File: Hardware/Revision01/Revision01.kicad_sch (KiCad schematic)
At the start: 6 parts, among them J5 Conn_01x02

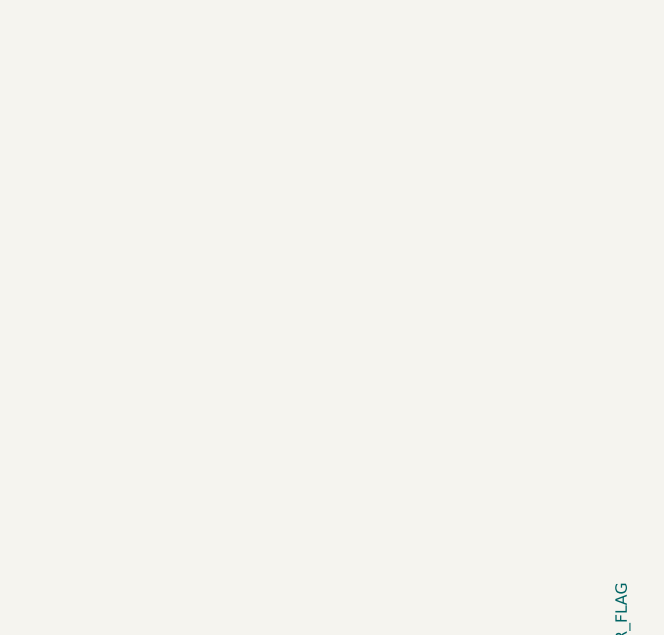
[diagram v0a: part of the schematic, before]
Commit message: footprint added for nucleo board
To do before PCB LAYOUT

clean up schematic
wire-accross sheets
Improve annotation ordering

Perform ERC check
Ensure all components have footprints
Create net classes
	POWER
	GND
	SPI
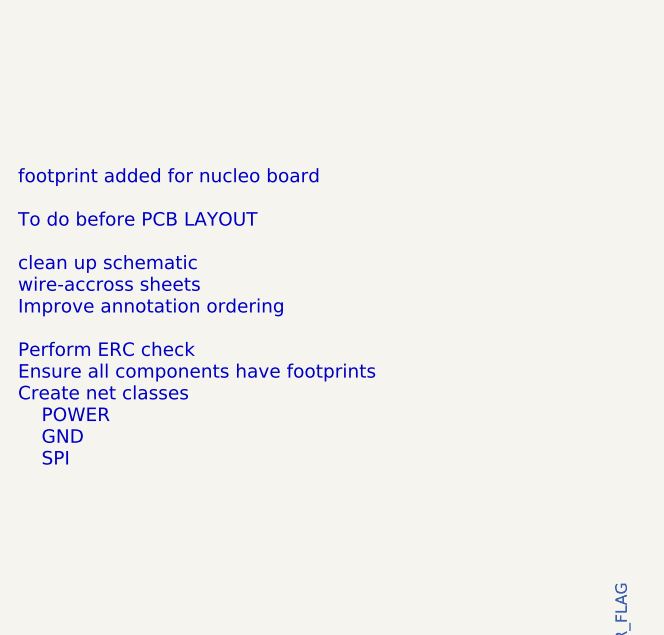
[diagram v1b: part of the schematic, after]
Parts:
- FID1, FID3: now in the parts list
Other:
- note added: "footprint added for nucleo board To do before PCB LAYOUT clean up schematic wire-accross sheets Improve annotation ordering Perform ERC check Ensure all components have footprints Create net classes POWER GND SPI"
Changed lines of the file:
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@@
 		(company "BCIT BAJA")
+	)
+	(text "\n\nfootprint added for nucleo board\n\nTo do before PCB LAYOUT\n\nclean up schematic\nwire-accross sheets\nImprove annotation ordering\n\nPerform ERC check\nEnsure all components have footprints\nCreate net classes\n	POWER\n	GND\n	SPI"
+		(exclude_from_sim no)
+		(at -45.466 99.568 0)
+		(effects
+			(font
+				(size 1.4986 1.4986)
+			)
+			(justify left)
+		)
 	)
 	(text "HOW MANY MOUNTING HOLES?"
@@
 		(at 161.29 189.23 0)
 		(unit 1)
-		(exclude_from_sim yes)
+		(exclude_from_sim no)
 		(in_bom no)
 		(on_board yes)
@@
 		(at 167.64 189.23 0)
 		(unit 1)
-		(exclude_from_sim yes)
-		(in_bom no)
+		(exclude_from_sim no)
+		(in_bom yes)
 		(on_board yes)
 		(dnp no)
@@
 		(at 153.67 189.23 0)
 		(unit 1)
-		(exclude_from_sim yes)
-		(in_bom no)
+		(exclude_from_sim no)
+		(in_bom yes)
 		(on_board yes)
 		(dnp no)

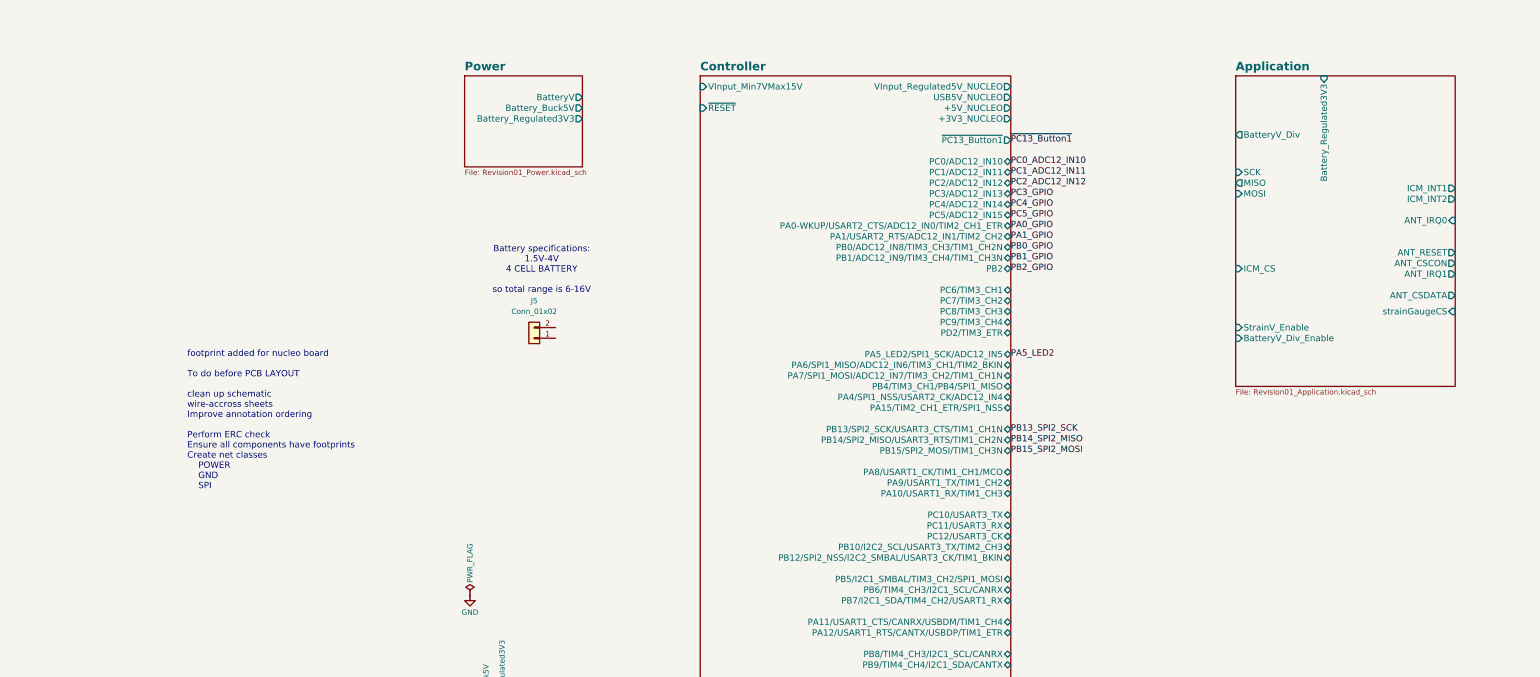
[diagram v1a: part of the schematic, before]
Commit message: started wiring modules together
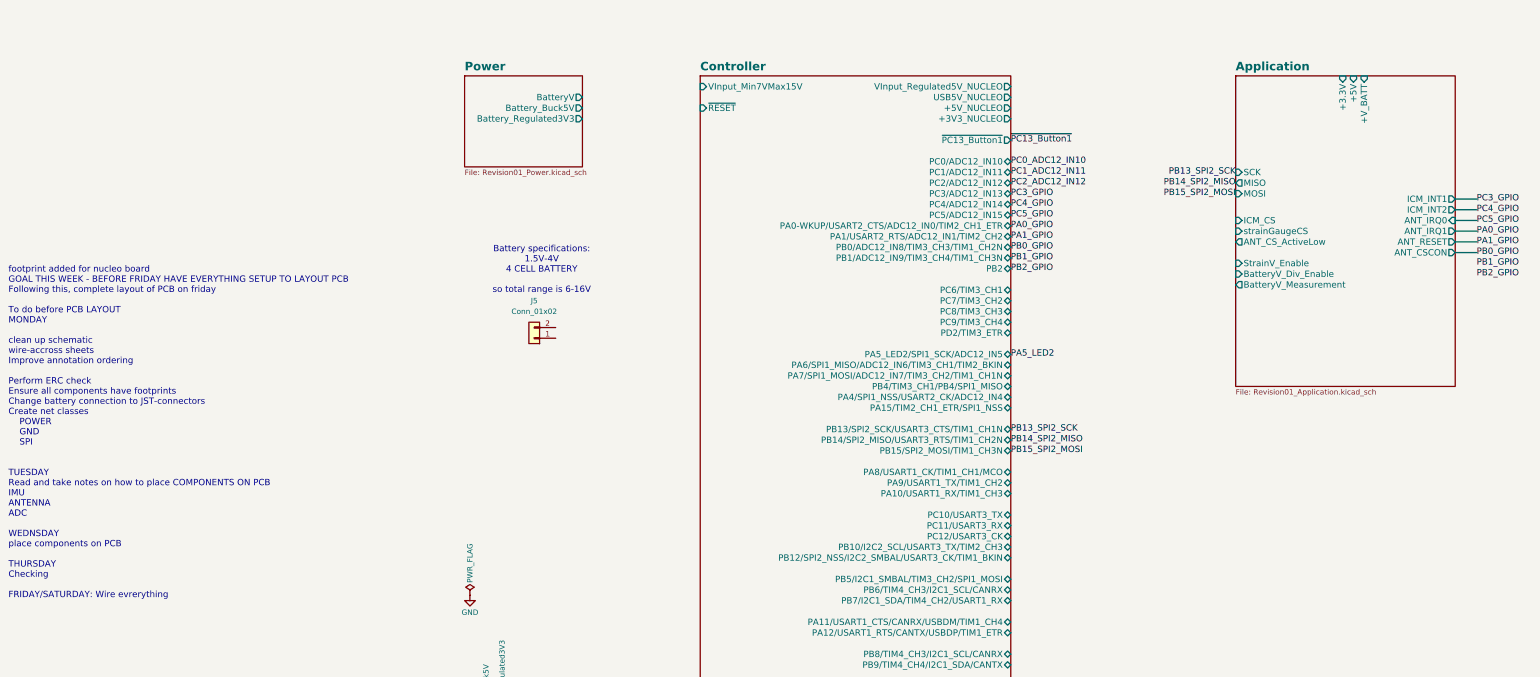
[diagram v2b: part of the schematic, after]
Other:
- sheet Application ports: added +3.3V, +5V, +V_BATT, ANT_CS_ActiveLow, BatteryV_Measurement; removed ANT_CSDATA, BatteryV_Div, Battery_Regulated3V3
- note added: "footprint added for nucleo board GOAL THIS WEEK - BEFORE FRIDAY HAVE EVERYTHING SETUP TO LAYOUT PCB Following this, complete layout of PCB on friday To do before PCB LAYOUT MONDAY clean up schematic wire-accross sheets Improve annotation ordering Perform ERC check Ensure all components have footprints Change battery connection to JST-connectors Create net classes POWER GND SPI TUESDAY Read and ta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"
- note removed: "footprint added for nucleo board To do before PCB LAYOUT clean up schematic wire-accross sheets Improve annotation ordering Perform ERC check Ensure all components have footprints Create net classes POWER GND SPI"
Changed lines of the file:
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@@
 		(company "BCIT BAJA")
 	)
-	(text "\n\nfootprint added for nucleo board\n\nTo do before PCB LAYOUT\n\nclean up schematic\nwire-accross sheets\nImprove annotation ordering\n\nPerform ERC check\nEnsure all components have footprints\nCreate net classes\n	POWER\n	GND\n	SPI"
-		(exclude_from_sim no)
-		(at -45.466 99.568 0)
+	(text "\n\nfootprint added for nucleo board\nGOAL THIS WEEK - BEFORE FRIDAY HAVE EVERYTHING SETUP TO LAYOUT PCB\nFollowing this, complete layout of PCB on friday\n\nTo do before PCB LAYOUT\nMONDAY\n\nclean up schematic\nwire-accross sheets\nImprove annotation ordering\n\nPerform ERC check\nEnsure all components have footprints\nChange battery connection to JST-connectors\nCreate net classes\n	POWER\n	GND\n	SPI\n\n\nTUESDAY\nRead and take notes on how to place COMPONENTS ON PCB\nIMU\nANTENNA\nADC\n\nWEDNSDAY \nplace components on PCB\n\nTHURSDAY\nChecking\n\nFRIDAY/SATURDAY: Wire evrerything\n\n\n"
+		(exclude_from_sim no)
+		(at -87.884 104.902 0)
 		(effects
 			(font
@@
 		(at 25.4 177.8)
 	)
+	(wire
+		(pts
+			(xy 260.35 59.69) (xy 255.27 59.69)
+		)
+		(stroke
+			(width 0)
+			(type default)
+		)
+	)
+	(wire
+		(pts
+			(xy 260.35 54.61) (xy 255.27 54.61)
+		)
+		(stroke
+			(width 0)
+			(type default)
+		)
+	)
+	(wire
+		(pts
+			(xy 260.35 57.15) (xy 255.27 57.15)
+		)
+		(stroke
+			(width 0)
+			(type default)
+		)
+	)
+	(wire
+		(pts
+			(xy 260.35 62.23) (xy 255.27 62.23)
+		)
+		(stroke
+			(width 0)
+			(type default)
+		)
+	)
+	(wire
+		(pts
+			(xy 260.35 49.53) (xy 255.27 49.53)
+		)
+		(stroke
+			(width 0)
+			(type default)
+		)
+	)
+	(wire
+		(pts
+			(xy 260.35 52.07) (xy 255.27 52.07)
+		)
+		(stroke
+			(width 0)
+			(type default)
+		)
+	)
 	(label "PC3_GPIO"
 		(at 149.86 48.26 0)
@@
 		)
 	)
+	(label "PB13_SPI2_SCK"
+		(at 203.2 43.18 180)
+		(effects
+			(font
+				(size 1.4986 1.4986)
+			)
+			(justify right)
+		)
+	)
 	(label "PB14_SPI2_MISO"
 		(at 149.86 106.68 0)
@@
 		)
 	)
+	(label "PA1_GPIO"
+		(at 260.35 59.69 0)
+		(effects
+			(font
+				(size 1.4986 1.4986)
+			)
+			(justify left)
+		)
+	)
+	(label "PC5_GPIO"
+		(at 260.35 54.61 0)
+		(effects
+			(font
+				(size 1.4986 1.4986)
+			)
+			(justify left)
+		)
+	)
+	(label "PA0_GPIO"
+		(at 260.35 57.15 0)
+		(effects
+			(font
+				(size 1.4986 1.4986)
+			)
+			(justify left)
+		)
+	)
+	(label "PB15_SPI2_MOSI"
+		(at 203.2 48.26 180)
+		(effects
+			(font
+				(size 1.4986 1.4986)
+			)
+			(justify right)
+		)
+	)
+	(label "PC4_GPIO"
+		(at 260.35 52.07 0)
+		(effects
+			(font
+				(size 1.4986 1.4986)
+			)
+			(justify left)
+		)
+	)
 	(label "PB0_GPIO"
 		(at 149.86 60.96 0)
@@
 		)
 	)
+	(label "PB14_SPI2_MISO"
+		(at 203.2 45.72 180)
+		(effects
+			(font
+				(size 1.4986 1.4986)
+			)
+			(justify right)
+		)
+	)
 	(label "PB1_GPIO"
 		(at 149.86 63.5 0)
@@
 		)
 	)
+	(label "PB2_GPIO"
+		(at 260.35 67.31 0)
+		(effects
+			(font
+				(size 1.4986 1.4986)
+			)
+			(justify left)
+		)
+	)
 	(label "PC0_ADC12_IN10"
 		(at 149.86 40.64 0)
@@
 		)
 	)
+	(label "PB0_GPIO"
+		(at 260.35 62.23 0)
+		(effects
+			(font
+				(size 1.4986 1.4986)
+			)
+			(justify left)
+		)
+	)
 	(label "PB2_GPIO"
 		(at 149.86 66.04 0)
@@
 	(label "PC1_ADC12_IN11"
 		(at 149.86 43.18 0)
+		(effects
+			(font
+				(size 1.4986 1.4986)
+			)
+			(justify left)
+		)
+	)
+	(label "PB1_GPIO"
+		(at 260.35 64.77 0)
+		(effects
+			(font
+				(size 1.4986 1.4986)
+			)
+			(justify left)
+		)
+	)
+	(label "PC3_GPIO"
+		(at 260.35 49.53 0)
 		(effects
 			(font
@@
 		)
 		(pin "ICM_INT1" output
-			(at 255.27 46.99 0)
+			(at 255.27 49.53 0)
 			(effects
 				(font
@@
 		)
 		(pin "ICM_INT2" output
-			(at 255.27 49.53 0)
+			(at 255.27 52.07 0)
 			(effects
 				(font
@@
 		)
 		(pin "ANT_RESET" output
+			(at 255.27 59.69 0)
+			(effects
+				(font
+					(size 1.4986 1.4986)
+				)
+				(justify right)
+			)
+		)
+		(pin "ANT_CSCON" output
 			(at 255.27 62.23 0)
 			(effects
@@
 			)
 		)
-		(pin "ANT_CSCON" output
-			(at 255.27 64.77 0)
-			(effects
-				(font
-					(size 1.4986 1.4986)
-				)
-				(justify right)
-			)
-		)
 		(pin "ANT_IRQ1" output
-			(at 255.27 67.31 0)
-			(effects
-				(font
-					(size 1.4986 1.4986)
-				)
-				(justify right)
-			)
-		)
-		(pin "ANT_CSDATA" output
-			(at 255.27 72.39 0)
+			(at 255.27 57.15 0)
 			(effects
 				(font
@@
 		)
 		(pin "strainGaugeCS" input
-			(at 255.27 76.2 0)
-			(effects
-				(font
-					(size 1.4986 1.4986)
-				)
-				(justify right)
-			)
-		)
-		(pin "Battery_Regulated3V3" input
-			(at 224.155 20.32 90)
-			(effects
-				(font
-					(size 1.4986 1.4986)
-				)
-				(justify right)
+			(at 203.2 57.15 180)
+			(effects
+				(font
+					(size 1.4986 1.4986)
+				)
+				(justify left)
 			)
 		)
 		(pin "ICM_CS" input
-			(at 203.2 66.04 180)
-			(effects
-				(font
-					(size 1.4986 1.4986)
-				)
-				(justify left)
-			)
-		)
-		(pin "BatteryV_Div" output
-			(at 203.2 34.29 180)
+			(at 203.2 54.61 180)
 			(effects
 				(font
@@
 		)
 		(pin "BatteryV_Div_Enable" input
-			(at 203.2 82.55 180)
+			(at 203.2 67.31 180)
 			(effects
 				(font
@@
 		)
 		(pin "StrainV_Enable" input
-			(at 203.2 80.01 180)
-			(effects
-				(font
+			(at 203.2 64.77 180)
+			(effects
+				(font
+					(size 1.4986 1.4986)
+				)
+				(justify left)
+			)
+		)
+		(pin "+3.3V" input
+			(at 228.6 20.32 90)
+			(effects
+				(font
+					(size 1.4986 1.4986)
+				)
+				(justify right)
+			)
+		)
+		(pin "+5V" input
+			(at 231.14 20.32 90)
+			(effects
+				(font
+					(size 1.4986 1.4986)
+				)
+				(justify right)
+			)
+		)
+		(pin "+V_BATT" input
+			(at 233.68 20.32 90)
+			(effects
+				(font
+					(size 1.4986 1.4986)
+				)
+				(justify right)
+			)
+		)
+		(pin "ANT_CS_ActiveLow" output
+			(at 203.2 59.69 180)
+			(effects
+				(font
+					(size 1.4986 1.4986)
+				)
+				(justify left)
+			)
+		)
+		(pin "BatteryV_Measurement" output
+			(at 203.2 69.85 180)
+			(effects
+				(font

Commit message: neated up the circuit - done wire-accross sheets - done Ensure all components have footprints - done Create net classes - DONE 	POWER 	GND 	SPI 	GPIO
Add in new components into BOM
	- Power switch, exclude from BOM - DONE - added component to switch. Not sure how to get it to work
	- Add in the resistors in parallel and series. for SPI busses - Done(PENDING whether to take series resistors out)
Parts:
- added H3, H4: MountingHole, MountingHole:MountingHole_3.2mm_M3, symbol Mechanical:MountingHole
- added R4, R5: 50, symbol Device:R
- added R6, R7: 10K, symbol Device:R
- added SW1: Power-switch connection, symbol Connector_Generic:Conn_01x02
- added TP16, TP17, TP18, TP19, TP8, TP9: TestPoint, TestPoint:TestPoint_THTPad_1.0x1.0mm_Drill0.5mm, symbol Connector:TestPoint
- H1, H2: footprint MountingHole:MountingHole_2.5mm -> MountingHole:MountingHole_3.2mm_M3
- J5: value Conn_01x02 -> Battery connector
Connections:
- net BatteryV: now also SW1.2 (Pin_2)
- net GND: now also J5.1 (Pin_1), TP19.1
- net at J5.2 (Pin_2): now also SW1.1 (Pin_1)
- new net +3.3V: R6.2, R7.2, TP8.1
- new net +5V: TP9.1
- new net Controller/PB14/SPI2_MISO/USART3_RTS/TIM1_CH2N: R4.1
- new net Controller/PB15/SPI2_MOSI/TIM1_CH3N: R5.1
- new net MISO: TP18.1
- new net MOSI: TP16.1
- new net SCK: TP17.1
- new net SPI_MISO: R4.2, R7.1
- new net SPI_MOSI: R5.2, R6.1
- no-connect marks 6 -> 7
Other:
- removed sheet Power
- sheet Application ports: added ANT_CSCON_AL, ANT_CS_DATA_AL; removed ANT_CSCON, ANT_CS_ActiveLow
- note added: "*Note this is externally connected wired to outside of case"
- note added: "These Mounting holes are M3"
- note added: "footprint added for nucleo board GOAL THIS WEEK - BEFORE FRIDAY HAVE EVERYTHING SETUP TO LAYOUT PCB Following this, complete layout of PCB on friday To do before PCB LAYOUT MONDAY Improve annotation ordering Perform ERC check TUESDAY Read and take notes on how to place COMPONENTS ON PCB IMU ANTENNA ADC WEDNSDAY place components on PCB THURSDAY Checking FRIDAY/SATURDAY: Wire evrerything"
- note removed: "HOW MANY MOUNTING HOLES?"
- note removed: "footprint added for nucleo board GOAL THIS WEEK - BEFORE FRIDAY HAVE EVERYTHING SETUP TO LAYOUT PCB Following this, complete layout of PCB on friday To do before PCB LAYOUT MONDAY clean up schematic wire-accross sheets Improve annotation ordering Perform ERC check Ensure all components have footprints Change battery connection to JST-connectors Create net classes POWER GND SPI TUESDAY Read and ta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"
- moved on the sheet: J5

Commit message: implemented feedback
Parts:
- removed R4, R5: 50, symbol Device:R
- removed R6, R7: 10K, symbol Device:R
- removed TP16, TP17, TP18, TP19: TestPoint, TestPoint:TestPoint_THTPad_1.0x1.0mm_Drill0.5mm, symbol Connector:TestPoint
- added TP12, TP13, TP14, TP15: TestPoint, TestPoint:TestPoint_THTPad_1.0x1.0mm_Drill0.5mm, symbol Connector:TestPoint
- SW1: now not fitted
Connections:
- net GND: now also TP15.1
- new net SPI2_MISO: TP14.1
- new net SPI2_MOSI: TP13.1
- new net SPI2_SCK: TP12.1
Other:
- note added: "footprint added for nucleo board GOAL THIS WEEK - BEFORE FRIDAY HAVE EVERYTHING SETUP TO LAYOUT PCB Following this, complete layout of PCB on friday To do before PCB LAYOUT MONDAY Improve annotation ordering Perform ERC check Move testpoints out of controller sheet TUESDAY Read and take notes on how to place COMPONENTS ON PCB IMU ANTENNA ADC WEDNSDAY place components on PCB THURSDAY Checking FRID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"
- note removed: "footprint added for nucleo board GOAL THIS WEEK - BEFORE FRIDAY HAVE EVERYTHING SETUP TO LAYOUT PCB Following this, complete layout of PCB on friday To do before PCB LAYOUT MONDAY Improve annotation ordering Perform ERC check TUESDAY Read and take notes on how to place COMPONENTS ON PCB IMU ANTENNA ADC WEDNSDAY place components on PCB THURSDAY Checking FRIDAY/SATURDAY: Wire evrerything"

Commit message: CREATE STM32CUBEIDE file to verify all ports Check over CONTROLLER SHEET Improve annotation ordering Move testpoints out of controller sheet
Still performering ERC check
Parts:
- added TP10, TP11, TP16, TP7, TP8, TP9: TestPoint, TestPoint:TestPoint_THTPad_1.0x1.0mm_Drill0.5mm, symbol Connector:TestPoint
- SW1: now fitted
- renumbered H3 to H2, H2 to H3, J5 to J1, TP8 to TP1, TP9 to TP2, TP12 to TP3, TP13 to TP4, TP14 to TP5, TP15 to TP6
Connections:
- new net Controller/BOOT0: TP7.1
- new net Controller/STLK_RX_USART2: TP8.1
- new net Controller/STLK_TX_USART2: TP9.1
- new net Controller/SWCLK: TP10.1
- new net Controller/SWDIO: TP11.1
- new net Controller/TRACESWO: TP16.1
- no-connect marks 7 -> 6
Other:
- sheet Application ports: added ANT_CSCON, ANT_CS_ActiveLow; removed ANT_CSCON_AL, ANT_CS_DATA_AL
- sheet Controller ports: added BOOT0, PB1, PC2, PC3, STLK_RX_USART2, STLK_TX_USART2, SWCLK, SWDIO, TRACESWO; removed PA10/USART1_RX/TIM1_CH3, PA11/USART1_CTS/CANRX/USBDM/TIM1_CH4, PA12/USART1_RTS/CANTX/USBDP/TIM1_ETR, PA15/TIM2_CH1_ETR/SPI1_NSS, PA4/SPI1_NSS/USART2_CK/ADC12_IN4, PA5_LED2/SPI1_SCK/ADC12_IN5, PA6/SPI1_MISO/ADC12_IN6/TIM3_CH1/TIM2_BKIN, PA7/SPI1_MOSI/ADC12_IN7/TIM3_CH2/TIM1_CH1N, PA8/USART1_CK/TIM1_CH1/MCO, PA9/USART1_TX/TIM1_CH2, PB10/I2C2_SCL/USART3_TX/TIM2_CH3, PB12/SPI2_NSS/I2C2_SMBAL/USART3_CK/TIM1_BKIN, PB1/ADC12_IN9/TIM3_CH4/TIM1_CH3N, PB4/TIM3_CH1/PB4/SPI1_MISO, PB5/I2C1_SMBAL/TIM3_CH2/SPI1_MOSI, PB6/TIM4_CH3/I2C1_SCL/CANRX, PB7/I2C1_SDA/TIM4_CH2/USART1_RX, PB8/TIM4_CH3/I2C1_SCL/CANRX, PB9/TIM4_CH4/I2C1_SDA/CANTX, PC10/USART3_TX, PC11/USART3_RX, PC12/USART3_CK, PC2/ADC12_IN12, PC3/ADC12_IN13, PC5/ADC12_IN15, PC6/TIM3_CH1, PC7/TIM3_CH2, PC8/TIM3_CH3, PC9/TIM3_CH4, PD2/TIM3_ETR, USB5V_NUCLEO, VInput_Regulated5V_NUCLEO, ~{PC13_Button1}, ~{RESET}
- note added: "footprint added for nucleo board GOAL THIS WEEK - BEFORE FRIDAY HAVE EVERYTHING SETUP TO LAYOUT PCB Following this, complete layout of PCB on friday CREATE STM32CUBEIDE file to verify all ports Check over CONTROLLER SHEET To do before PCB LAYOUT MONDAY Improve annotation ordering Perform ERC check Move testpoints out of controller sheet TUESDAY Read and take notes on how to place COMPONENTS ON PC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"
- note removed: "footprint added for nucleo board GOAL THIS WEEK - BEFORE FRIDAY HAVE EVERYTHING SETUP TO LAYOUT PCB Following this, complete layout of PCB on friday To do before PCB LAYOUT MONDAY Improve annotation ordering Perform ERC check Move testpoints out of controller sheet TUESDAY Read and take notes on how to place COMPONENTS ON PCB IMU ANTENNA ADC WEDNSDAY place components on PCB THURSDAY Checking FRID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"
